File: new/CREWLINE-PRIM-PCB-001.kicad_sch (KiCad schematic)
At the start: 76 parts, among them J1 BATTERY, J10 ESTOP INPUTS, J2 CHARGE SHIELD HEADER, J3 DIO, J4 PWR INPUTS, J5 CAN CABLES, J6 SEAT_CONNECTOR, J7 BRAKE INPUTS, J8 SAFETY_CONNECTOR, J9 Conn_02x06_Counter_Clockwise, Q1 IRF4905STRL

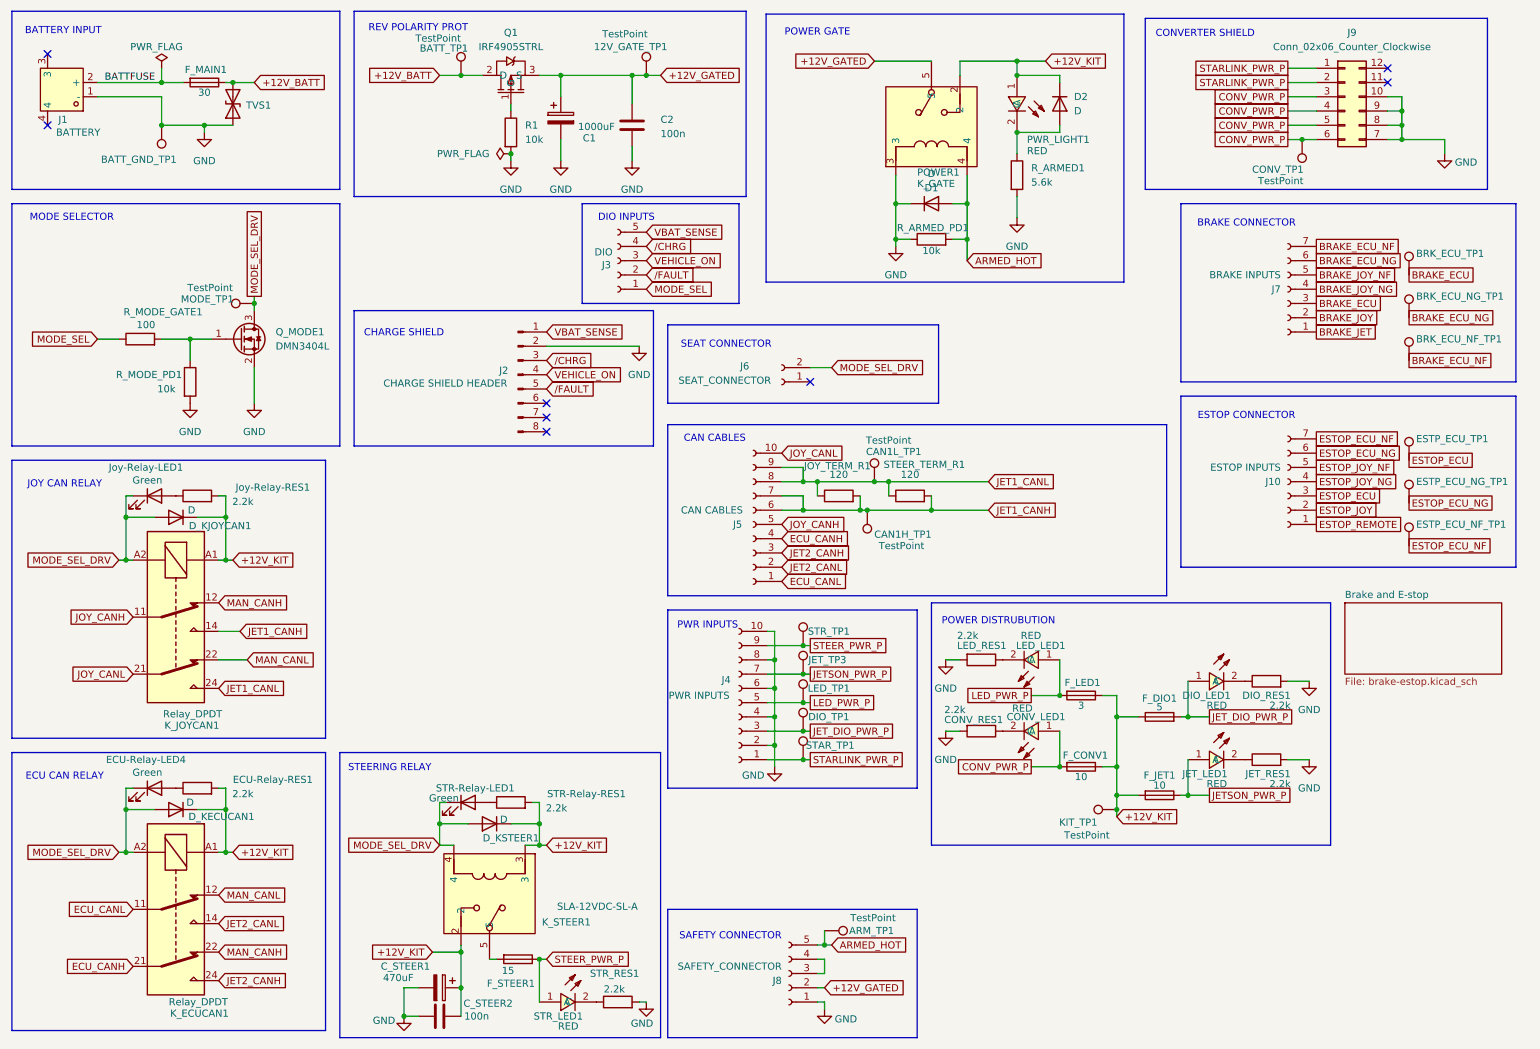
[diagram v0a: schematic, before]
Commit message: Apply the routine findings of the independent review
Via sizes now follow the net class, and +12V_GATED and +12V_KIT are
re-routed with them. Relay references sit below the relay bodies with
a 0.15 mm stroke. The mounting holes are H1 to H4, board-only, on a
rectangular pattern. Diodes carry the value 1N4148WS. The README
records the re-routed nets, the disabled checks and the open items.
Derived files regenerated.

Co-Authored-By: Claude Fable 5.1 <noreply@anthropic.com>
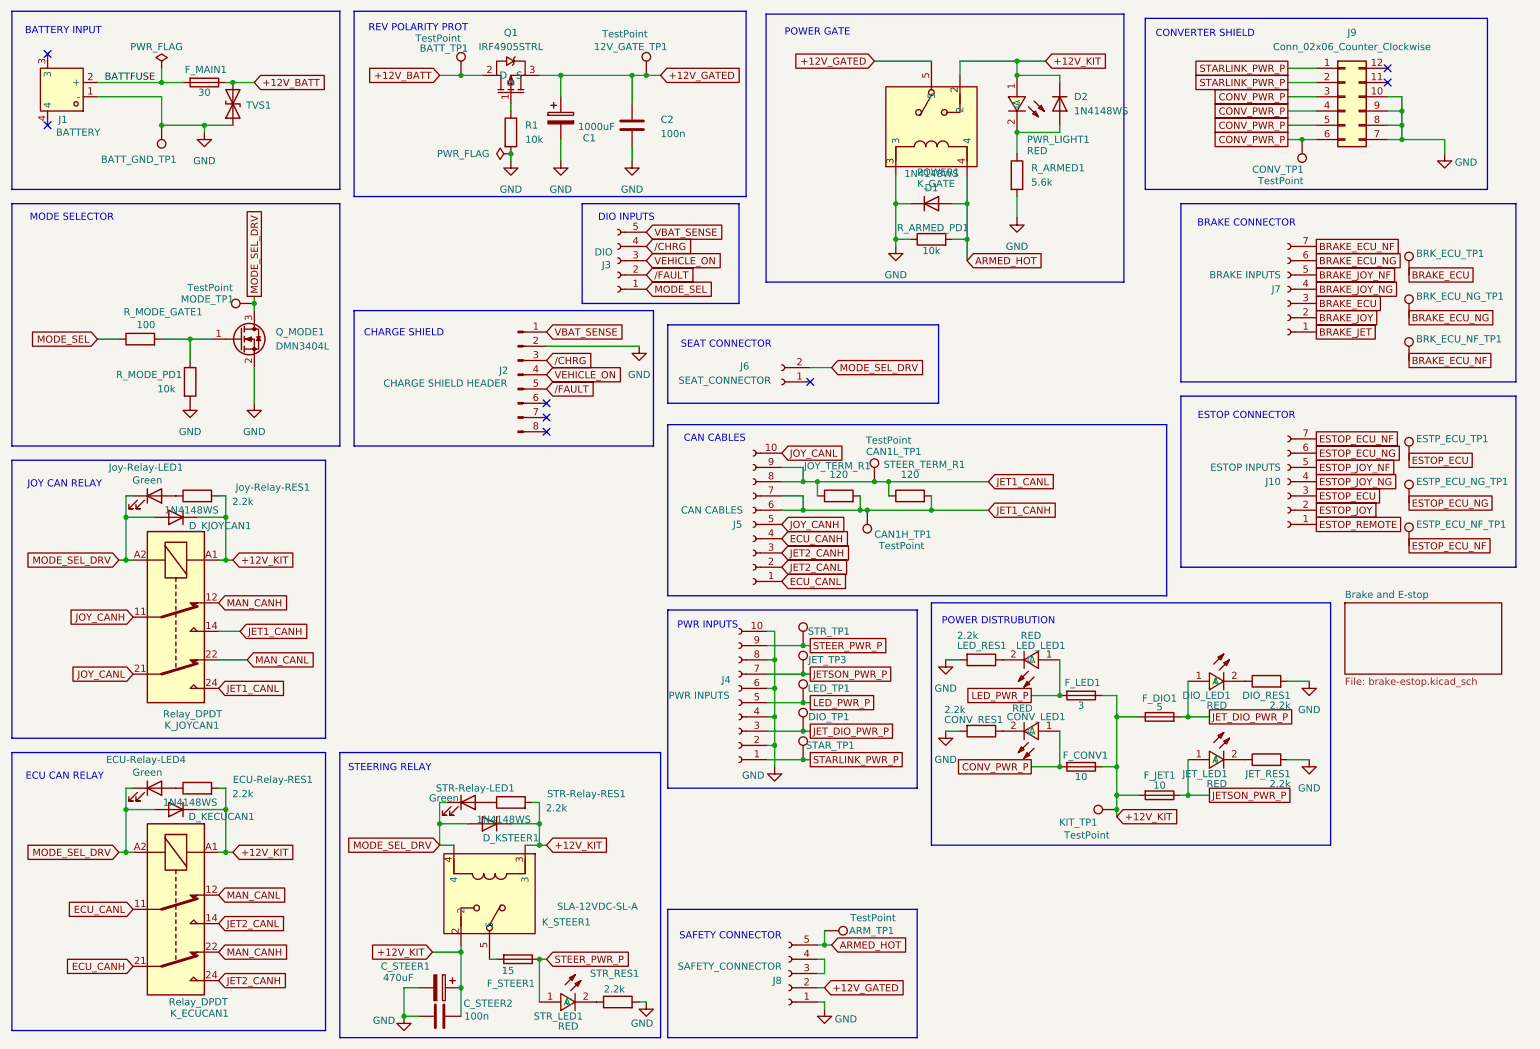
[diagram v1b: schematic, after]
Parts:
- D1, D2, D_KECUCAN1, D_KJOYCAN1, D_KSTEER1: value D -> 1N4148WS
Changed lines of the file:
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@@
 			)
 		)
-		(property "Value" "D"
+		(property "Value" "1N4148WS"
 			(at 45.974 102.87 0)
 			(show_name no)
@@
 			)
 		)
-		(property "Value" "D"
+		(property "Value" "1N4148WS"
 			(at 101.6 157.988 0)
 			(show_name no)
@@
 			)
 		)
-		(property "Value" "D"
+		(property "Value" "1N4148WS"
 			(at 45.72 154.94 0)
 			(show_name no)
@@
 			)
 		)
-		(property "Value" "D"
+		(property "Value" "1N4148WS"
 			(at 177.8 42.926 0)
 			(show_name no)
@@
 			)
 		)
-		(property "Value" "D"
+		(property "Value" "1N4148WS"
 			(at 203.2 31.7499 90)
 			(show_name no)
